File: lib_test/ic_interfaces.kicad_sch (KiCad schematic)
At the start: 1 part, among them U13001 SN75176

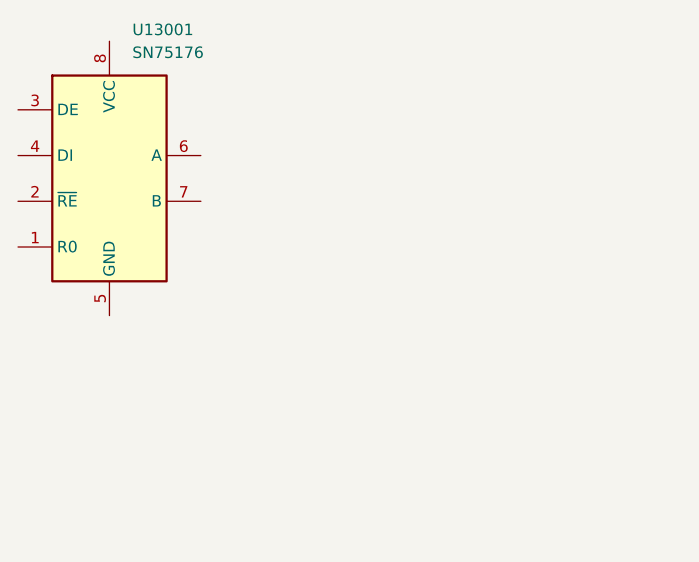
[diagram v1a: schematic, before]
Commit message: add FT231
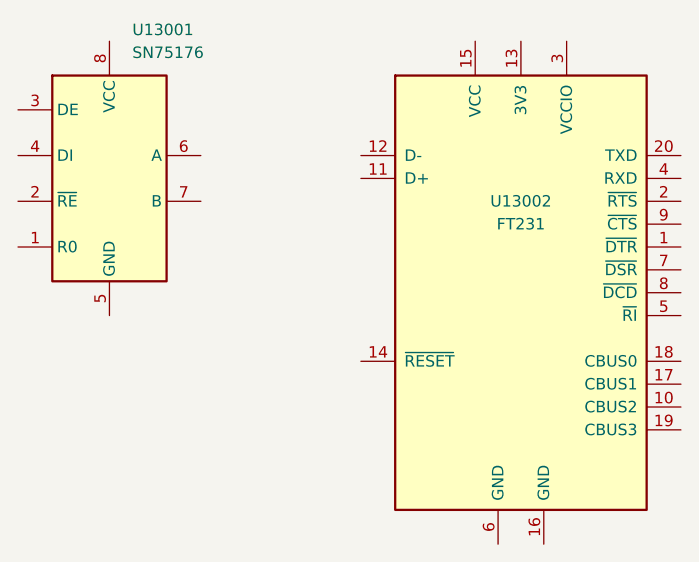
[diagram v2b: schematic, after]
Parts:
- added U13002: FT231, lily_footprints:ssop20_pitch25_341x154_mil, symbol lily_symbols:ic_usb_to_serial_FT231_ssop20
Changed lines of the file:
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@@
+		)
+	)
+	(symbol
+		(lib_id "lily_symbols:ic_usb_to_serial_FT231_ssop20")
+		(at 63.5 38.1 0)
+		(unit 1)
+		(exclude_from_sim no)
+		(in_bom yes)
+		(on_board yes)
+		(dnp no)
+		(property "Reference" "U13002"
+			(at 81.28 43.18 0)
+			(effects
+				(font
+					(size 1.27 1.27)
+				)
+			)
+		)
+		(property "Value" "FT231"
+			(at 81.28 45.72 0)
+			(effects
+				(font
+					(size 1.27 1.27)
+				)
+			)
+		)
+		(property "Footprint" "lily_footprints:ssop20_pitch25_341x154_mil"
+			(at 81.28 99.06 0)
+			(effects
+				(font
+					(size 1.27 1.27)
+				)
+				(hide yes)
+			)
+		)
+		(property "Datasheet" ""
+			(at 63.5 38.1 0)
+			(effects
+				(font
+					(size 1.27 1.27)
+				)
+				(hide yes)
+			)
+		)
+		(property "Description" ""
+			(at 63.5 38.1 0)
+			(effects
+				(font
+					(size 1.27 1.27)
+				)
+				(hide yes)
+			)
+		)
+		(property "Revision" "1"
+			(at 81.28 93.98 0)
+			(effects
+				(font
+					(size 1.27 1.27)
+				)
+				(hide yes)
+			)
+		)
+		(property "Status" "Active"
+			(at 81.28 96.52 0)
+			(effects
+				(font
+					(size 1.27 1.27)
+				)
+				(hide yes)
+			)
+		)
+		(property "Manufacturer" "FTDI"
+			(at 81.28 101.6 0)
+			(effects
+				(font
+					(size 1.27 1.27)
+				)
+				(hide yes)
+			)
+		)
+		(property "Manufacturer_ID" "FT231XS-R"
+			(at 81.28 104.14 0)
+			(effects
+				(font
+					(size 1.27 1.27)
+				)
+				(hide yes)
+			)
+		)
+		(property "Lily_ID" "1914-10002"
+			(at 81.28 106.68 0)
+			(effects
+				(font
+					(size 1.27 1.27)
+				)
+				(hide yes)
+			)
+		)
+		(property "JLCPCB_ID" "C132160"
+			(at 81.28 109.22 0)
+			(effects
+				(font
+					(size 1.27 1.27)
+				)
+				(hide yes)
+			)
+		)
+		(property "JLCPCB_STATUS" "Extended"
+			(at 81.28 111.76 0)
+			(effects
+				(font
+					(size 1.27 1.27)
+				)
+				(hide yes)
+			)
+		)
+		(pin "13"
+		)
+		(pin "16"
+		)
+		(pin "19"
+		)
+		(pin "5"
+		)
+		(pin "12"
+		)
+		(pin "4"
+		)
+		(pin "10"
+		)
+		(pin "7"
+		)
+		(pin "6"
+		)
+		(pin "8"
+		)
+		(pin "9"
+		)
+		(pin "2"
+		)
+		(pin "1"
+		)
+		(pin "11"
+		)
+		(pin "3"
+		)
+		(pin "14"
+		)
+		(pin "17"
+		)
+		(pin "20"
+		)
+		(pin "18"
+		)
+		(pin "15"
+		)
+		(instances
+			(project "kicad_lib_test"
+				(path "/032b8f2d-5c08-4381-9e3a-c197ca84e3c5/e12ad61a-1df8-4431-b529-c2075b837a06"
+					(reference "U13002")
+					(unit 1)
+				)
+			)
 		)
 	)
